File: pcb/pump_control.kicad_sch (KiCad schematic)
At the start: 2 parts, among them J6 Screw_Terminal_01x02, K1 SANYOU_SRD_Form_A

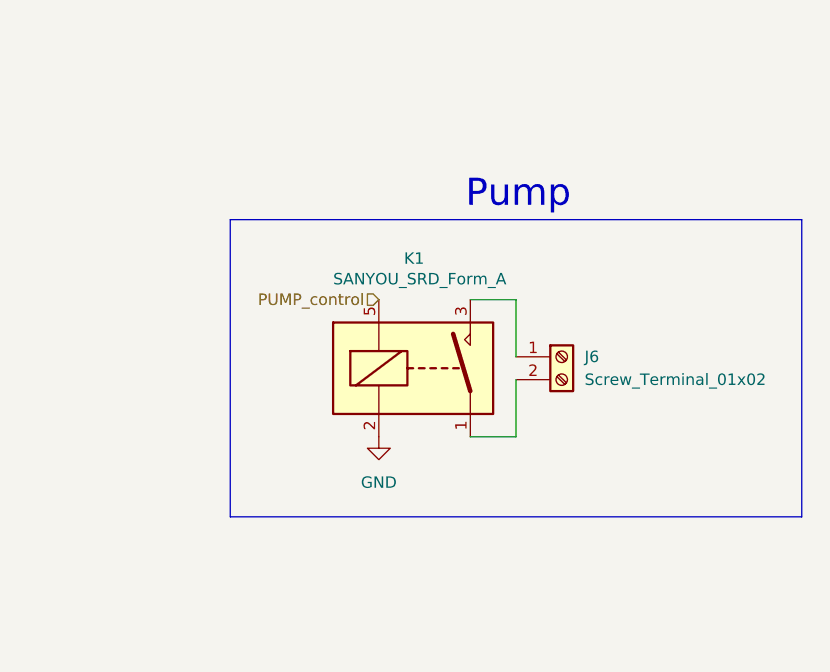
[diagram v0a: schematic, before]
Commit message: redesigning the circuit of the rellay and starting to adjust the footprints
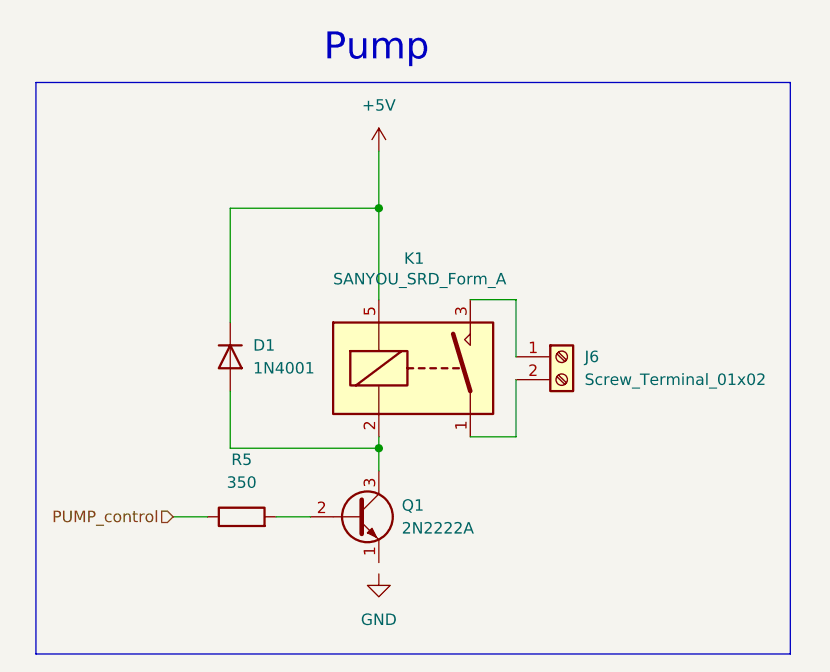
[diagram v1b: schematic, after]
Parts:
- added D1: 1N4001, Diode_THT:D_DO-41_SOD81_P10.16mm_Horizontal, symbol Diode:1N4001
- added Q1: 2N2222A, Package_TO_SOT_THT:TO-39-3, symbol Transistor_BJT:2N3904
- added R5: 350, symbol Device:R
- J6: footprint (none) -> TerminalBlock_Phoenix:TerminalBlock_Phoenix_MKDS-1,5-2_1x02_P5.00mm_Horizontal; amazon link (none) -> https://www.amazon.com/QSYZAIL-Screw-Terminal-Circuit-Conne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
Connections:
- net GND: no longer K1.2
- net PUMP_control: now also R5.1; no longer K1.5
- new net: D1.2 (A), K1.2, Q1.3 (C)
- new net: Q1.2 (B), R5.2
- new net +5V: D1.1 (K), K1.5

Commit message: finishing the bom and adding the jlc number of the parts
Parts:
- D1: jlc part # (none) -> C2456
- J6: jlc part # (none) -> C3703
- K1: footprint Relay_THT:Relay_SPST_SANYOU_SRD_Series_Form_A -> Relay_THT:Relay_SPDT_SANYOU_SRD_Series_Form_C; amazon link (none) -> https://www.amazon.com/Weasch-SRD-05VDC-SL-C-250VAC-Househo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; jlc part # (none) -> C35449
- Q1: amazon link (none) -> https://www.amazon.com/100Pcs-2N2222-2N2222A-MPS2222-Triode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; jlc part # (none) -> C118536
- R5: footprint (none) -> Resistor_SMD:R_0603_1608Metric_Pad0.98x0.95mm_HandSolder; amazon link (none) -> https://www.amazon.com/1500PCS-Resistor-Values-Tolerance-As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; jlc part # (none) -> C100982
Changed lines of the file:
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@@
+			)
+		)
+		(property "jlc part #" "C2456"
+			(at 123.19 93.98 90)
+			(effects
+				(font
+					(size 1.27 1.27)
+				)
+				(hide yes)
 			)
 		)
@@
 			)
 		)
+		(property "amazon link" "https://www.amazon.com/100Pcs-2N2222-2N2222A-MPS2222-Triode/dp/B0H6G1CLJM?"
+			(at 137.16 111.76 0)
+			(effects
+				(font
+					(size 1.27 1.27)
+				)
+				(hide yes)
+			)
+		)
+		(property "jlc part #" "C118536"
+			(at 137.16 111.76 0)
+			(effects
+				(font
+					(size 1.27 1.27)
+				)
+				(hide yes)
+			)
+		)
 		(pin "1"
 		)
@@
 			)
 		)
-		(property "Footprint" "Relay_THT:Relay_SPST_SANYOU_SRD_Series_Form_A"
+		(property "Footprint" "Relay_THT:Relay_SPDT_SANYOU_SRD_Series_Form_C"
 			(at 153.67 96.52 0)
 			(effects
@@
 			)
 		)
-		(property "amazon link" ""
+		(property "amazon link" "https://www.amazon.com/Weasch-SRD-05VDC-SL-C-250VAC-Household-Appliance/dp/B0D2MRY3BT?crid=6RMELHQI7PLL"
+			(at 144.78 95.25 0)
+			(effects
+				(font
+					(size 1.27 1.27)
+				)
+				(hide yes)
+			)
+		)
+		(property "jlc part #" "C35449"
 			(at 144.78 95.25 0)
 			(effects
@@
 			)
 		)
+		(property "jlc part #" "C3703"
+			(at 160.02 93.98 0)
+			(effects
+				(font
+					(size 1.27 1.27)
+				)
+				(hide yes)
+			)
+		)
 		(pin "2"
 		)
@@
 			)
 		)
-		(property "Footprint" ""
+		(property "Footprint" "Resistor_SMD:R_0603_1608Metric_Pad0.98x0.95mm_HandSolder"
 			(at 124.46 113.538 90)
 			(effects
@@
 			(effects
 				(font
+					(size 1.27 1.27)
+				)
+				(hide yes)
+			)
+		)
+		(property "amazon link" "https://www.amazon.com/1500PCS-Resistor-Values-Tolerance-Assorted/dp/B09537D852"
+			(at 124.46 111.76 90)
+			(effects
+				(font
+					(size 1.27 1.27)
+				)
+				(hide yes)
+			)
+		)
+		(property "jlc part #" "C100982"
+			(at 124.46 111.76 90)
+			(effects
+				(font

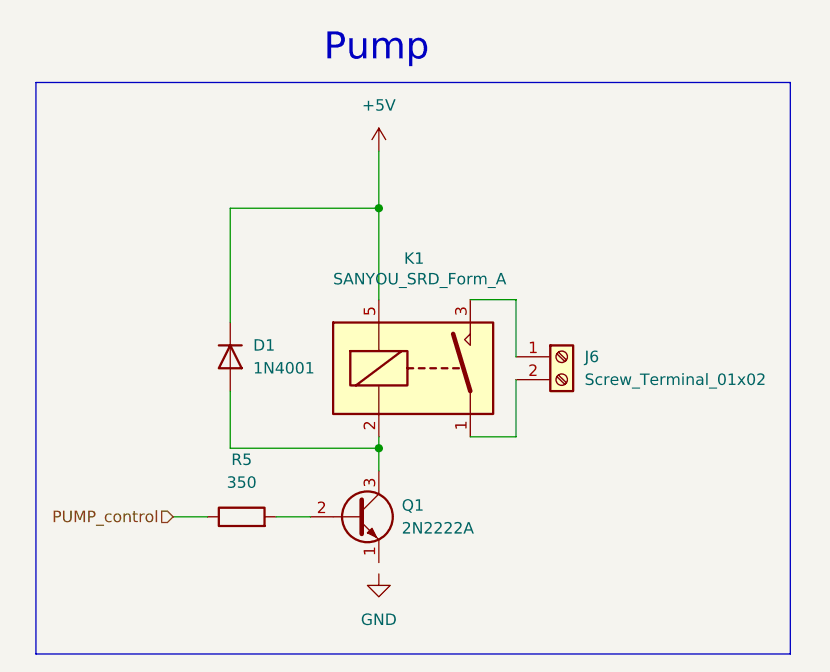
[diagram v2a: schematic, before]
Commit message: placing the components
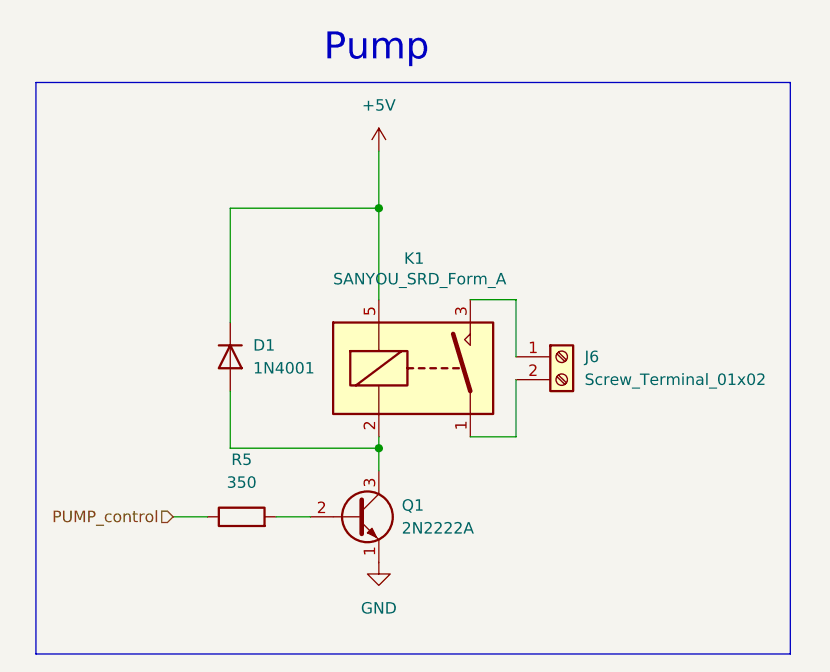
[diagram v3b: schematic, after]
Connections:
- net GND: now also Q1.1 (E)
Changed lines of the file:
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@@
 	(symbol
 		(lib_id "power:GND")
-		(at 139.7 118.11 0)
+		(at 139.7 116.84 0)
 		(unit 1)
 		(exclude_from_sim no)
@@
 		(fields_autoplaced yes)
 		(property "Reference" "#PWR013"
-			(at 139.7 124.46 0)
+			(at 139.7 123.19 0)
 			(effects
 				(font
@@
 		)
 		(property "Value" "GND"
-			(at 139.7 123.19 0)
+			(at 139.7 121.92 0)
 			(effects
 				(font
@@
 		)
 		(property "Footprint" ""
-			(at 139.7 118.11 0)
+			(at 139.7 116.84 0)
 			(effects
 				(font
@@
 		)
 		(property "Datasheet" ""
-			(at 139.7 118.11 0)
+			(at 139.7 116.84 0)
 			(effects
 				(font
@@
 		)
 		(property "Description" "Power symbol creates a global label with name \"GND\" , ground"
-			(at 139.7 118.11 0)
+			(at 139.7 116.84 0)
 			(effects
 				(font

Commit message: separating the pcb components from the other BOM
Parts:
- J6: amazon link https://www.amazon.com/QSYZAIL-Screw-Terminal-Circuit-Conne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 -> (none)
- K1: amazon link https://www.amazon.com/Weasch-SRD-05VDC-SL-C-250VAC-Househo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 -> (none)
- Q1: amazon link https://www.amazon.com/100Pcs-2N2222-2N2222A-MPS2222-Triode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 -> (none)
- R5: amazon link https://www.amazon.com/1500PCS-Resistor-Values-Tolerance-As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 -> (none)
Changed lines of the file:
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@@
-			)
-		)
-		(property "amazon link" "https://www.amazon.com/100Pcs-2N2222-2N2222A-MPS2222-Triode/dp/B0H6G1CLJM?"
-			(at 137.16 111.76 0)
-			(effects
-				(font
-					(size 1.27 1.27)
-				)
-				(hide yes)
 			)
 		)
@@
 		)
 		(property "Description" "Sanyo SRD relay, Single Pole Miniature Power Relay, Closing Contact"
-			(at 144.78 95.25 0)
-			(effects
-				(font
-					(size 1.27 1.27)
-				)
-				(hide yes)
-			)
-		)
-		(property "amazon link" "https://www.amazon.com/Weasch-SRD-05VDC-SL-C-250VAC-Household-Appliance/dp/B0D2MRY3BT?crid=6RMELHQI7PLL"
 			(at 144.78 95.25 0)
 			(effects
@@
 			)
 		)
-		(property "amazon link" "https://www.amazon.com/QSYZAIL-Screw-Terminal-Circuit-Connector/dp/B0G4MYNHBC/132-4224079-3597343"
-			(at 160.02 93.98 0)
-			(effects
-				(font
-					(size 1.27 1.27)
-				)
-				(hide yes)
-			)
-		)
 		(property "jlc part #" "C3703"
 			(at 160.02 93.98 0)
@@
 			(effects
 				(font
-					(size 1.27 1.27)
-				)
-				(hide yes)
-			)
-		)
-		(property "amazon link" "https://www.amazon.com/1500PCS-Resistor-Values-Tolerance-Assorted/dp/B09537D852"
-			(at 124.46 111.76 90)
-			(effects
-				(font
